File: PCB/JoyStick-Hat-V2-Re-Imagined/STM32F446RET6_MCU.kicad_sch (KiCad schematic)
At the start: 64 parts, among them J1 20021121-00010C4LF, J10 0901301212, J12 DX07S016JA1R1500, J2 BU2032SM-JJ-GTR, J3 0901301210, J7 SBH11-PBPC-D10-ST-BK, SW1 PTS636 SM43 SMTR LFS, U1 STM32F446VETx, X1 ABM3B-8.000MHZ-B2-T, X2 ABS07-32.768KHZ-9-T

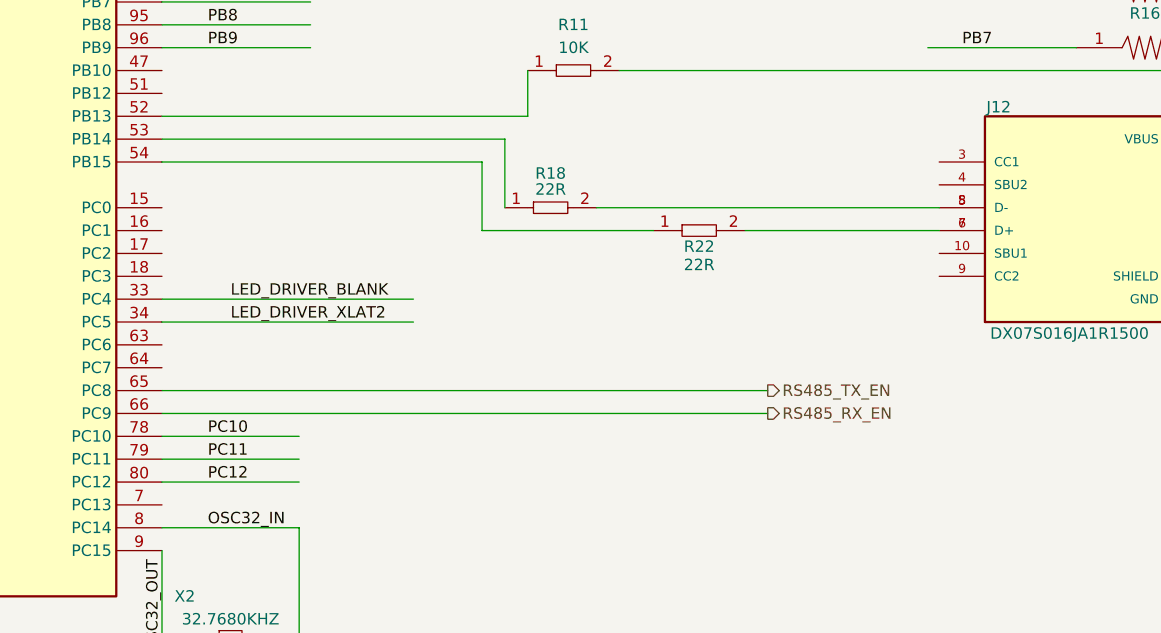
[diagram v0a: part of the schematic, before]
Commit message: Fab Fixes
Fixing for Frabrication, DRC cleared by pending external review subject to change.
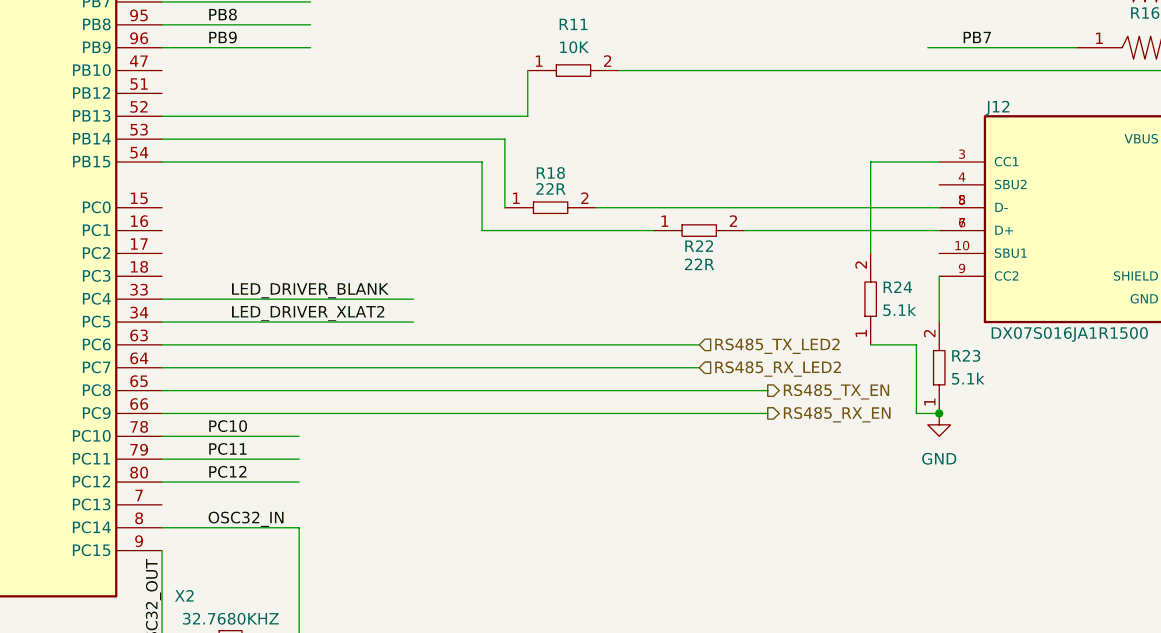
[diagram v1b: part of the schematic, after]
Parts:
- added R23, R24: RC0402FR-075K1L, AVR-KiCAD-Lib-Resistors:R0402, symbol AVR-KiCAD-Lib-Resistors:RC0402FR-075K1L
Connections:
- net GND: now also R23.1, R24.1
- net at J12.3 (CC1): now also R24.2
- net at J12.9 (CC2): now also R23.2
- net RS485_TX_LED2: now reaches U1.63 (PC6)
- net RS485_RX_LED2: now reaches U1.64 (PC7)

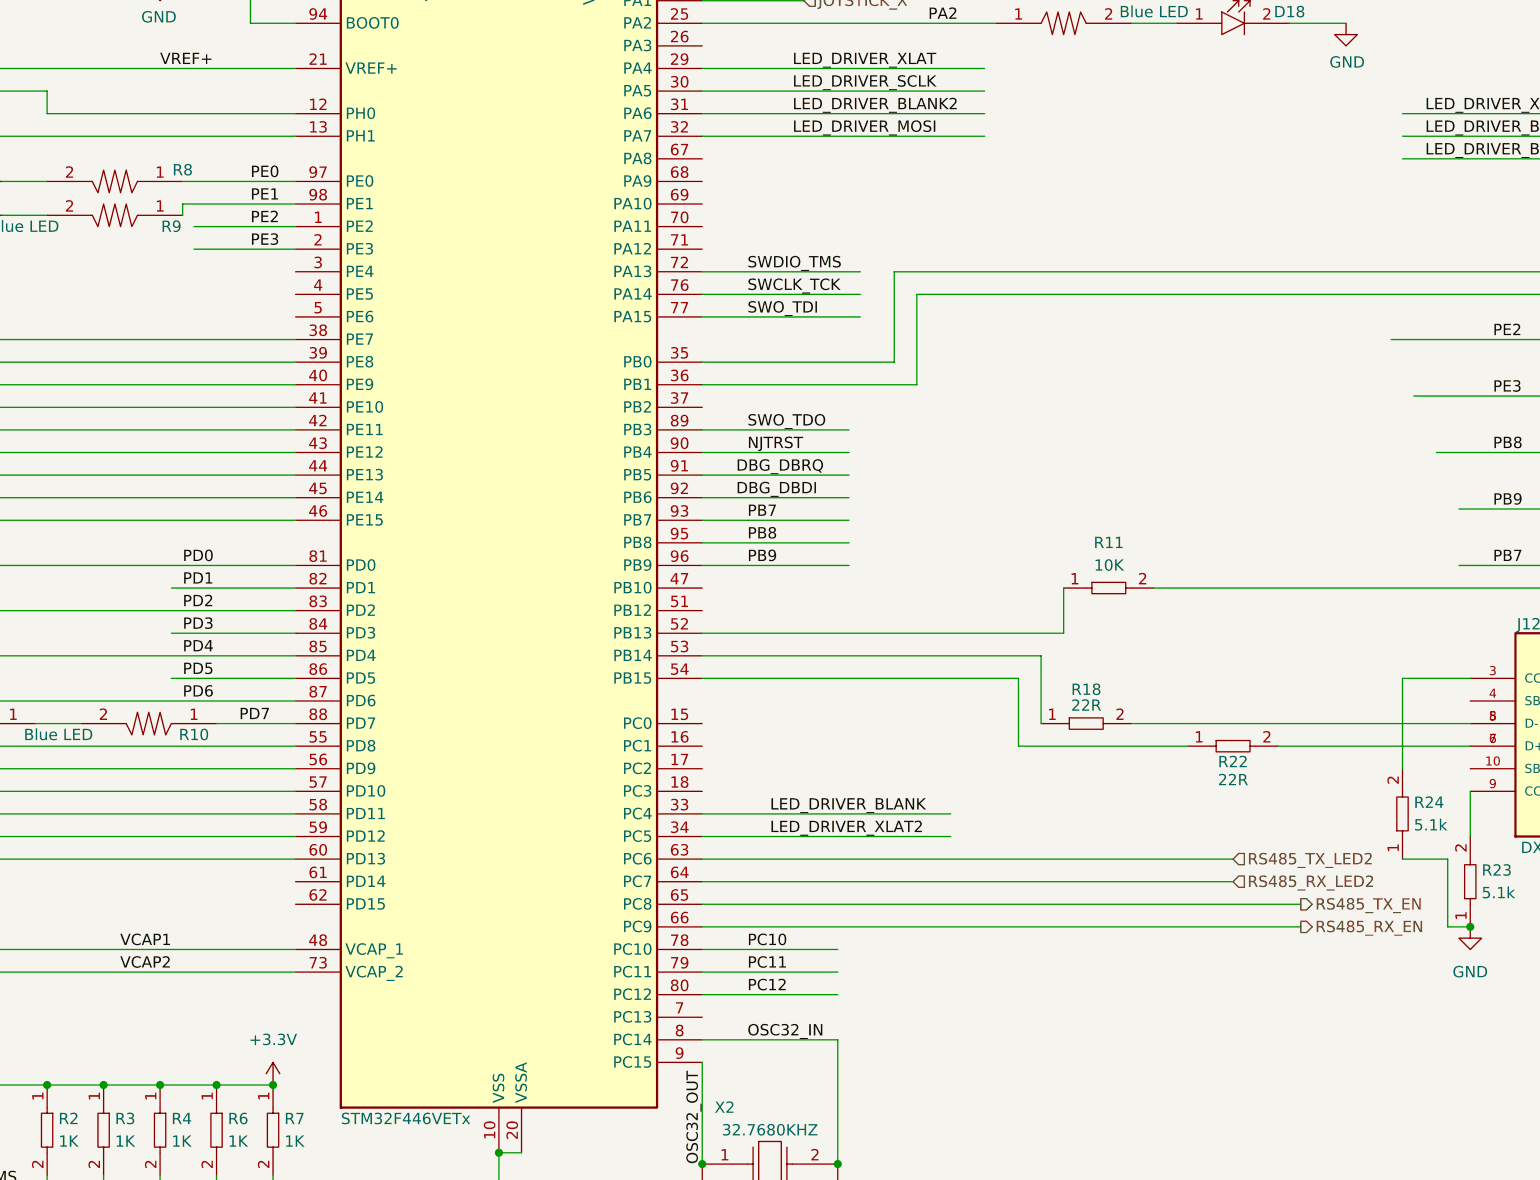
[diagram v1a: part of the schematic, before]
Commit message: STM32 Exp
Removed 5V regulator, corrected RS485 schematic,  added more expansion to STM32 since we had space.
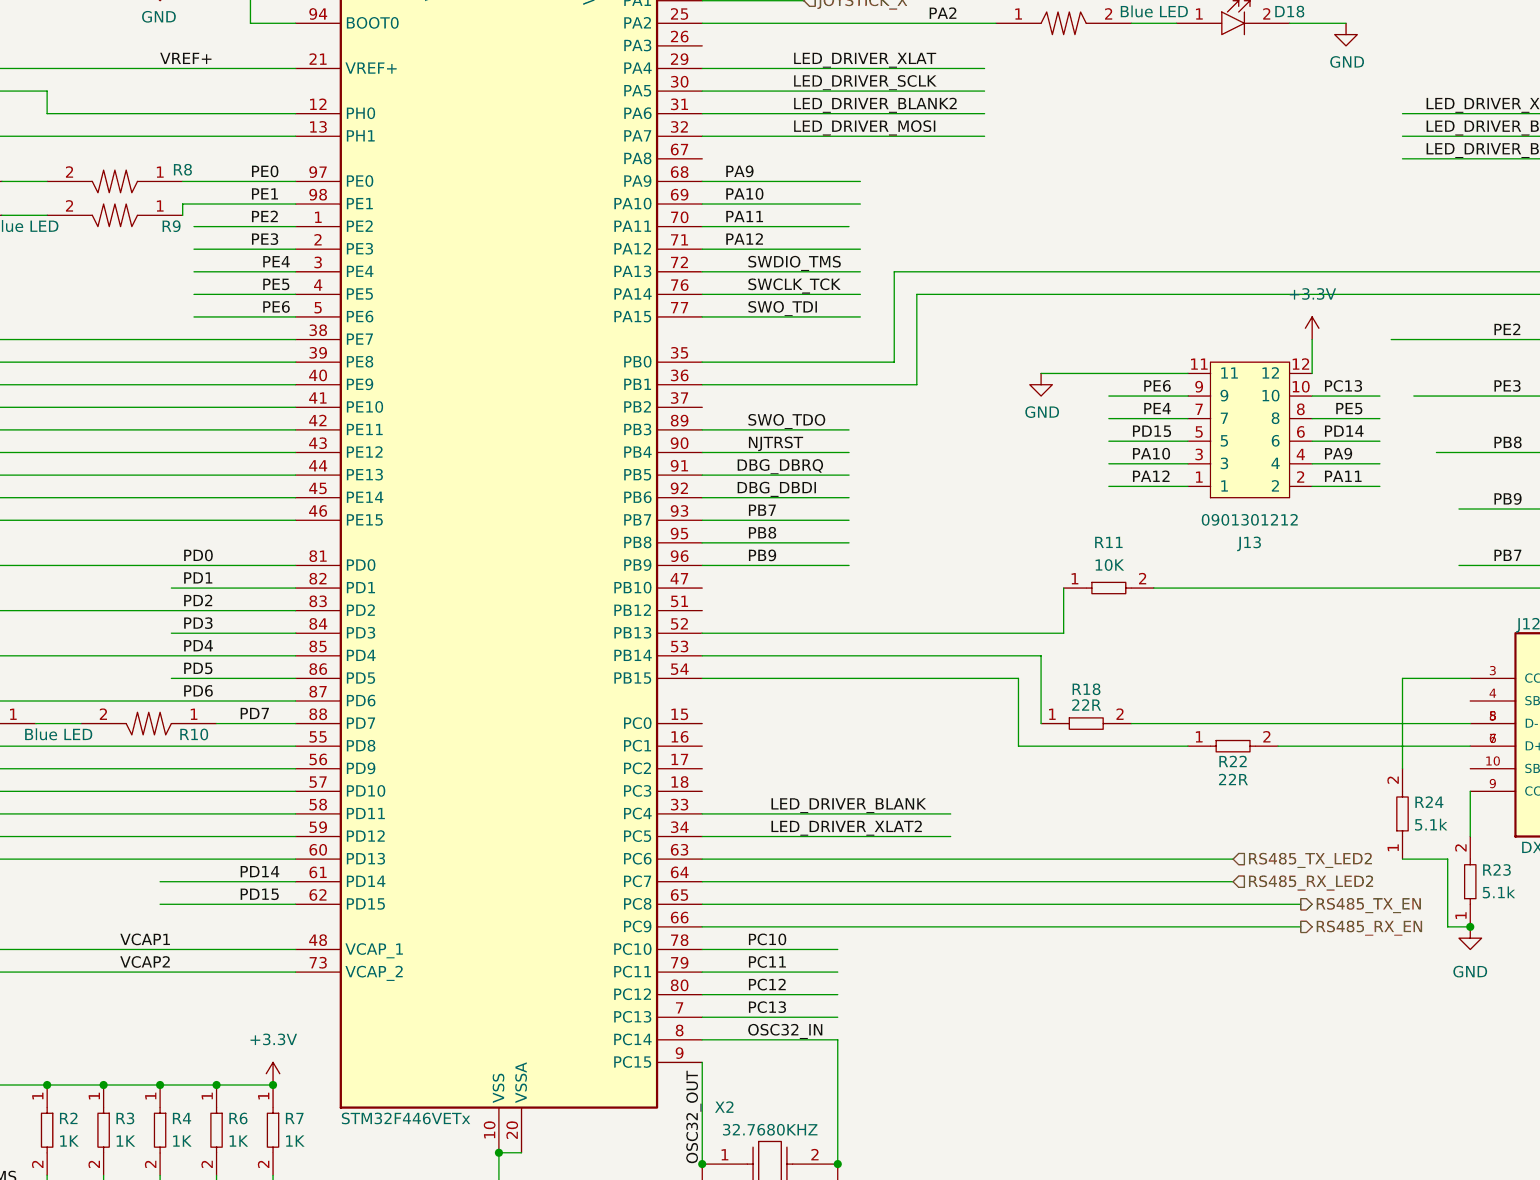
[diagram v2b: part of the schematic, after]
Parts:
- added J13: 0901301212, AVR-KiCAD-Lib-Connectors:CON_901301212_MOL, symbol AVR-KiCAD-Lib-Connectors:0901301212
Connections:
- net +3.3V: now also J13.12
- net GND: now also J13.11
- net PE4: now reaches U1.3 (PE4)
- net PE4: now also J13.7
- net PE5: now reaches U1.4 (PE5)
- net PE5: now also J13.8
- net PE6: now reaches U1.5 (PE6)
- net PE6: now also J13.9
- net PD14: now reaches U1.61 (PD14)
- net PD14: now also J13.6
- net PD15: now reaches U1.62 (PD15)
- net PD15: now also J13.5
- net PA9: now reaches U1.68 (PA9)
- net PA9: now also J13.4
- net PA10: now reaches U1.69 (PA10)
- net PA10: now also J13.3
- net PC13: now reaches U1.7 (PC13)
- net PC13: now also J13.10
- net PA11: now reaches U1.70 (PA11)
- net PA11: now also J13.2
- net PA12: now reaches U1.71 (PA12)
- net PA12: now also J13.1

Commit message: RS485 Circuit Fixes, STM32 Expansion
Fixe RS485 circuit errors, changed PCB topology for RS485. Added STM32 expansion IO in place of 5V Regulator.
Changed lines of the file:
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@@
 	(wire
 		(pts
-			(xy 137.16 149.86) (xy 204.47 149.86)
+			(xy 137.16 149.86) (xy 196.85 149.86)
 		)
 		(stroke
@@
 	(wire
 		(pts
-			(xy 137.16 152.4) (xy 204.47 152.4)
+			(xy 137.16 152.4) (xy 196.85 152.4)
 		)
 		(stroke
@@
 	)
 	(label "PE5"
-		(at 87.63 81.28 0)
+		(at 86.36 81.28 0)
 		(fields_autoplaced yes)
 		(effects
@@
 	)
 	(label "PE6"
-		(at 87.63 83.82 0)
+		(at 86.36 83.82 0)
 		(fields_autoplaced yes)
 		(effects
@@
 	)
 	(label "PA11"
-		(at 139.7 73.66 0)
+		(at 142.24 73.66 0)
 		(fields_autoplaced yes)
 		(effects
@@
 	)
 	(label "PE4"
-		(at 87.63 78.74 0)
+		(at 86.36 78.74 0)
 		(fields_autoplaced yes)
 		(effects
@@
 	)
 	(label "PA12"
-		(at 139.7 76.2 0)
+		(at 142.24 76.2 0)
 		(fields_autoplaced yes)
 		(effects
@@
 	)
 	(label "PA10"
-		(at 139.7 71.12 0)
+		(at 142.24 71.12 0)
 		(fields_autoplaced yes)
 		(effects
@@
 	)
 	(label "PA9"
-		(at 139.7 68.58 0)
+		(at 142.24 68.58 0)
 		(fields_autoplaced yes)
 		(effects
@@
 	(hierarchical_label "RS485_TX_EN"
 		(shape output)
-		(at 204.47 149.86 0)
+		(at 196.85 149.86 0)
 		(fields_autoplaced yes)
 		(effects
@@
 	(hierarchical_label "RS485_RX_EN"
 		(shape output)
-		(at 204.47 152.4 0)
+		(at 196.85 152.4 0)
 		(fields_autoplaced yes)
 		(effects
@@
 		(on_board yes)
 		(dnp no)
-		(fields_autoplaced yes)
 		(property "Reference" "J10"
-			(at 29.845 105.41 0)
+			(at 26.924 109.474 0)
 			(effects
 				(font
@@
 		)
 		(property "Value" "0901301212"
-			(at 29.845 107.95 0)
+			(at 29.464 127 0)
 			(effects
 				(font
